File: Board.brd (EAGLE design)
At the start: 0 parts

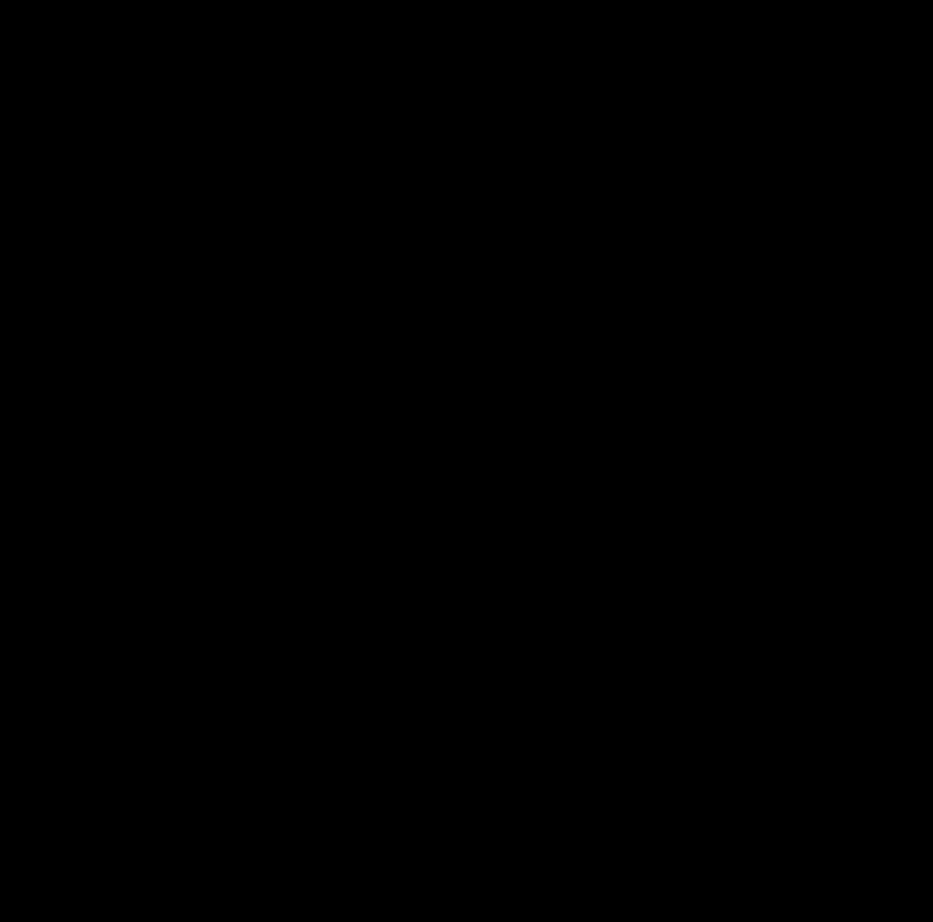
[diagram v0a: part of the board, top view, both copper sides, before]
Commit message: add m5 atom martix component
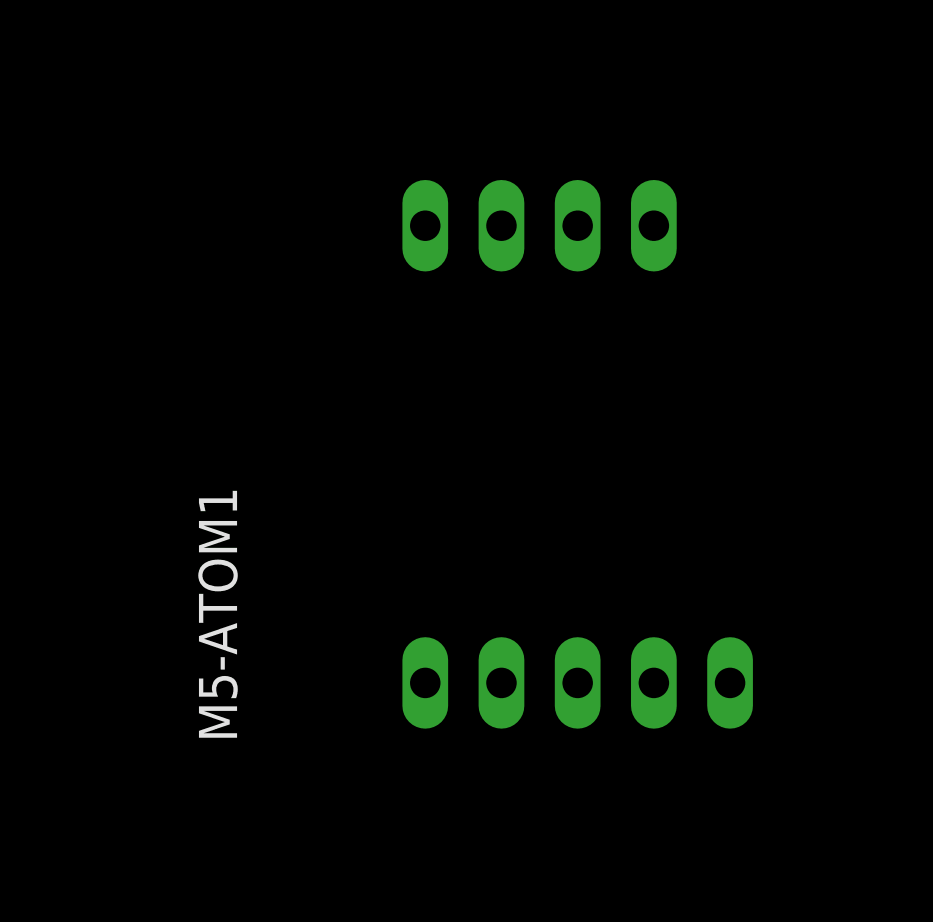
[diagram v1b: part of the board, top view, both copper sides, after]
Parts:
- added M5-ATOM1: (no value), Design-by-Amri:M5-ATOM-MATRIX
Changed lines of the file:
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@@
 <setting verticaltext="up"/>
 </settings>
-<grid distance="0.05" unitdist="inch" unit="inch" style="lines" multiple="1" display="yes" altdistance="0.025" altunitdist="inch" altunit="inch"/>
+<grid distance="25" unitdist="mil" unit="mil" style="lines" multiple="1" display="yes" altdistance="0.025" altunitdist="inch" altunit="inch"/>
 <layers>
 <layer number="1" name="Top" color="4" fill="1" visible="yes" active="yes"/>
@@
 <layer number="25" name="tNames" color="7" fill="1" visible="yes" active="yes"/>
 <layer number="26" name="bNames" color="7" fill="1" visible="yes" active="yes"/>
-<layer number="27" name="tValues" color="7" fill="1" visible="yes" active="yes"/>
-<layer number="28" name="bValues" color="7" fill="1" visible="yes" active="yes"/>
-<layer number="29" name="tStop" color="7" fill="3" visible="yes" active="yes"/>
-<layer number="30" name="bStop" color="7" fill="6" visible="yes" active="yes"/>
-<layer number="31" name="tCream" color="7" fill="4" visible="yes" active="yes"/>
-<layer number="32" name="bCream" color="7" fill="5" visible="yes" active="yes"/>
-<layer number="33" name="tFinish" color="6" fill="3" visible="yes" active="yes"/>
-<layer number="34" name="bFinish" color="6" fill="6" visible="yes" active="yes"/>
-<layer number="35" name="tGlue" color="7" fill="4" visible="yes" active="yes"/>
-<layer number="36" name="bGlue" color="7" fill="5" visible="yes" active="yes"/>
-<layer number="37" name="tTest" color="7" fill="1" visible="yes" active="yes"/>
-<layer number="38" name="bTest" color="7" fill="1" visible="yes" active="yes"/>
+<layer number="27" name="tValues" color="7" fill="1" visible="no" active="yes"/>
+<layer number="28" name="bValues" color="7" fill="1" visible="no" active="yes"/>
+<layer number="29" name="tStop" color="7" fill="3" visible="no" active="yes"/>
+<layer number="30" name="bStop" color="7" fill="6" visible="no" active="yes"/>
+<layer number="31" name="tCream" color="7" fill="4" visible="no" active="yes"/>
+<layer number="32" name="bCream" color="7" fill="5" visible="no" active="yes"/>
+<layer number="33" name="tFinish" color="6" fill="3" visible="no" active="yes"/>
+<layer number="34" name="bFinish" color="6" fill="6" visible="no" active="yes"/>
+<layer number="35" name="tGlue" color="7" fill="4" visible="no" active="yes"/>
+<layer number="36" name="bGlue" color="7" fill="5" visible="no" active="yes"/>
+<layer number="37" name="tTest" color="7" fill="1" visible="no" active="yes"/>
+<layer number="38" name="bTest" color="7" fill="1" visible="no" active="yes"/>
 <layer number="39" name="tKeepout" color="4" fill="11" visible="yes" active="yes"/>
 <layer number="40" name="bKeepout" color="1" fill="11" visible="yes" active="yes"/>
 <layer number="41" name="tRestrict" color="4" fill="10" visible="yes" active="yes"/>
 <layer number="42" name="bRestrict" color="1" fill="10" visible="yes" active="yes"/>
-<layer number="43" name="vRestrict" color="2" fill="10" visible="yes" active="yes"/>
-<layer number="44" name="Drills" color="7" fill="1" visible="yes" active="yes"/>
-<layer number="45" name="Holes" color="7" fill="1" visible="yes" active="yes"/>
-<layer number="46" name="Milling" color="3" fill="1" visible="yes" active="yes"/>
-<layer number="47" name="Measures" color="7" fill="1" visible="yes" active="yes"/>
+<layer number="43" name="vRestrict" color="2" fill="10" visible="no" active="yes"/>
+<layer number="44" name="Drills" color="7" fill="1" visible="no" active="yes"/>
+<layer number="45" name="Holes" color="7" fill="1" visible="no" active="yes"/>
+<layer number="46" name="Milling" color="3" fill="1" visible="no" active="yes"/>
+<layer number="47" name="Measures" color="7" fill="1" visible="no" active="yes"/>
 <layer number="48" name="Document" color="7" fill="1" visible="yes" active="yes"/>
-<layer number="49" name="Reference" color="7" fill="1" visible="yes" active="yes"/>
+<layer number="49" name="Reference" color="7" fill="1" visible="no" active="yes"/>
 <layer number="51" name="tDocu" color="7" fill="1" visible="yes" active="yes"/>
 <layer number="52" name="bDocu" color="7" fill="1" visible="yes" active="yes"/>
+<layer number="88" name="SimResults" color="9" fill="1" visible="no" active="no"/>
+<layer number="89" name="SimProbes" color="9" fill="1" visible="no" active="no"/>
 <layer number="90" name="Modules" color="5" fill="1" visible="no" active="no"/>
 <layer number="91" name="Nets" color="2" fill="1" visible="no" active="no"/>
@@
 </autorouter>
 <elements>
+<element name="M5-ATOM1" library="Design-by-Amri" package="M5-ATOM-MATRIX" value="" x="105.41" y="32.385" smashed="yes" rot="R90">
+<attribute name="NAME" x="91.5162" y="22.7838" size="1.27" layer="25" ratio="10" rot="R90"/>
+<attribute name="VALUE" x="93.345" y="22.86" size="1.27" layer="27" rot="R90"/>
+</element>
 </elements>
 <signals>
